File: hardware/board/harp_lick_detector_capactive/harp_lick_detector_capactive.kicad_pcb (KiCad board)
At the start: 2 copper layers, 90 x 60 mm, 119 parts, among them J1 USB_C_Receptacle_USB2.0, J10 Conn_01x02_Male, J2 Conn_01x03_Male, J3 Conn_01x03_Male, J4 AudioJack3, J5 Barrel_Jack_Switch, J6 Conn_Coaxial, J7 Conn_Coaxial, J8 Conn_Coaxial, J9 Conn_Coaxial, U10 LTC6263, U11 CD74AC04, U2 W25Q128JVS, U3 ADUM4160, U4 TPD2EUSB30, U5 LT3030, U6 LM27762, U7 AD9833xRM, U8 LTC6263, U9 LTC6268xS6-10, X1 ECS-TXO-2016, X2 ASE-25.000MHZ-L-C-T

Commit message: loosely place components
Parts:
- removed REF** (x4): MountingHole_3.2mm_M3_DIN965, MountingHole:MountingHole_3.2mm_M3_DIN965
- added U1: RP2040, machine_agency_components:RP2040-QFN-56, F.Cu at (197.0, 79.8)
- C10, C11, C12, C13, C14, C17, C18, C19, C20, C21, C22, C23, C24, C27, C28, C29, C30, C32, C33, C34, C35, C36: footprint Capacitor_SMD:C_0603_1608Metric_Pad1.08x0.95mm_HandSolder -> Capacitor_SMD:C_0402_1005Metric_Pad0.74x0.62mm_HandSolder
- moved R20 205.3 mm to (226.5, 62.5), turned to 180 degrees
- moved R32 198.2 mm to (240.2, 102.0), turned to 180 degrees
- moved R31 196.5 mm to (240.2, 97.4), turned to 180 degrees
- moved D3 193.1 mm to (230.0, 75.0)
- moved R4 191.8 mm to (223.1, 88.1)
- moved C10 184.7 mm to (219.2, 86.0), turned to 90 degrees
- moved R8 183.3 mm to (205.7, 80.5), turned to 180 degrees
- moved R7 183.0 mm to (220.0, 81.5), turned to 180 degrees
- moved C16 181.8 mm to (222.0, 98.6), turned to 180 degrees
- moved C36 177.9 mm to (219.8, 50.9)
- moved R22 175.0 mm to (226.5, 75.0), turned to 180 degrees
- moved R5 174.3 mm to (221.4, 75.1), turned to 180 degrees
- moved C22 174.0 mm to (215.7, 50.8)
- moved C108 173.7 mm to (202.9, 78.6)
- moved R6 173.2 mm to (220.0, 80.5), turned to 180 degrees
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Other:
- board size 90 x 60 mm -> 68 x 60 mm

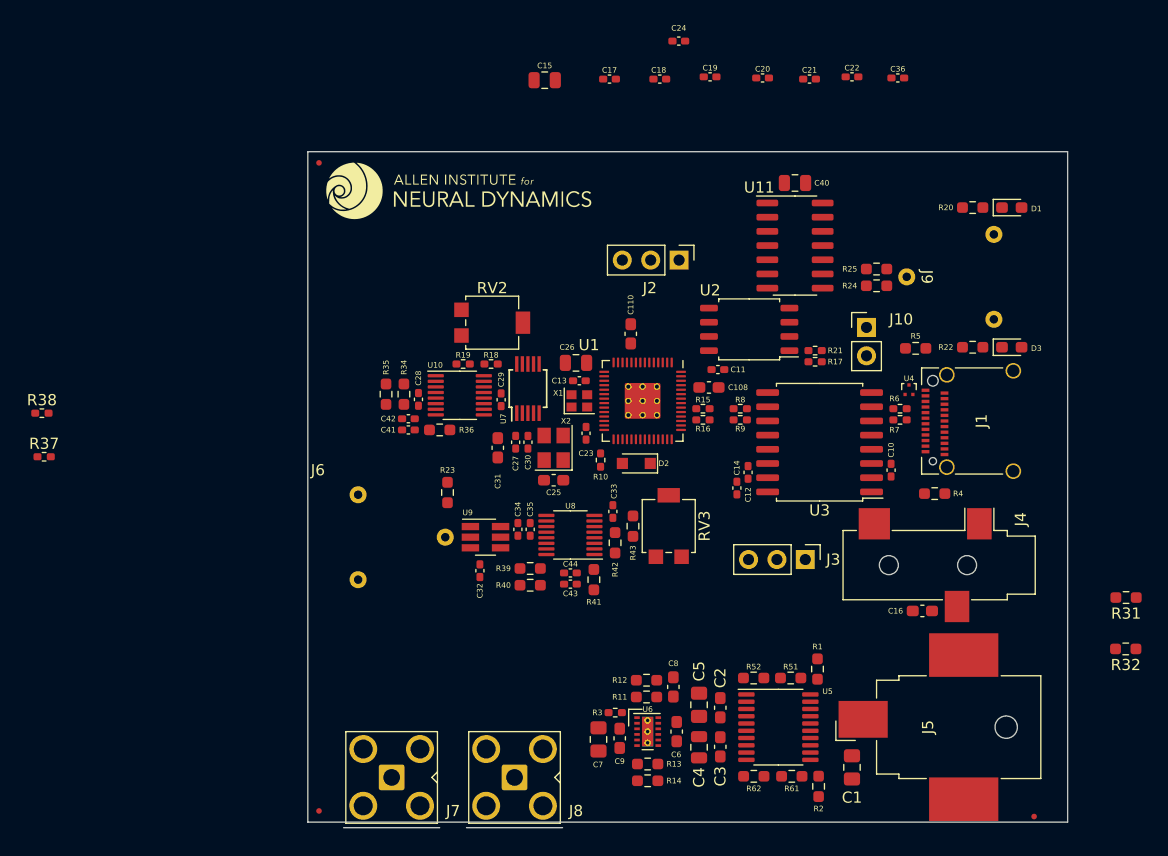
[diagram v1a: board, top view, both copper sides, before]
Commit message: change usb connector; more layout
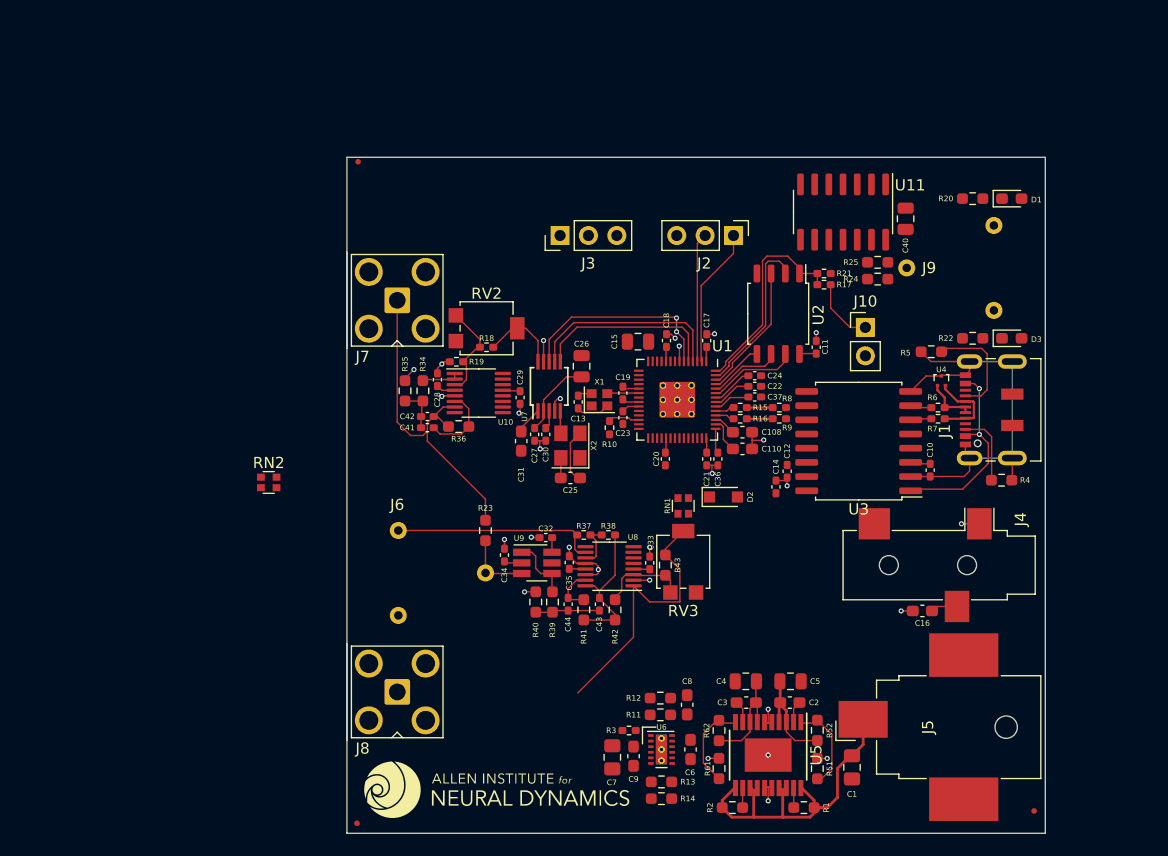
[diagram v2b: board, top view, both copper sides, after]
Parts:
- removed R31, R32: 4K7, Resistor_SMD:R_0603_1608Metric_Pad0.98x0.95mm_HandSolder
- added C37: 100nF, Capacitor_SMD:C_0402_1005Metric_Pad0.74x0.62mm_HandSolder, F.Cu at (207.0, 79.5)
- added RN1: 5K, Resistor_SMD:R_Array_Convex_2x0606, F.Cu at (200.6, 89.2)
- added RN2: 5K, Resistor_SMD:R_Array_Convex_2x0606, F.Cu at (163.5, 87.1)
- C5: footprint Capacitor_SMD:C_0805_2012Metric_Pad1.18x1.45mm_HandSolder -> Capacitor_SMD:C_0805_2012Metric
- J1: footprint Connector_USB:USB_C_Receptacle_Amphenol_12401610E4-2A_CircularHoles -> Connector_USB:USB_C_Receptacle_JAE_DX07S016JA1R1500
- U5: footprint Package_SO:TSSOP-20_4.4x6.5mm_P0.65mm -> Package_SO:ETSSOP-20-1EP_4.4x6.5mm_P0.65mm_EP3x4.2mm
- moved G*** 53.7 mm to (183.9, 114.6)
- moved R38 51.9 mm to (193.9, 91.8)
- moved R37 48.8 mm to (191.7, 91.8), turned to 180 degrees
- moved J7 42.7 mm to (175.0, 70.8), turned to 90 degrees
- moved C36 37.7 mm to (203.7, 85.0), turned to 90 degrees
- moved J3 36.4 mm to (189.6, 65.0), turned to 90 degrees
- moved C21 35.2 mm to (202.7, 85.0), turned to 90 degrees
- moved C20 35.2 mm to (199.0, 85.0), turned to 90 degrees
- moved C24 30.7 mm to (207.0, 77.5), turned to 180 degrees
- moved C19 29.4 mm to (195.2, 79.1), turned to -90 degrees
- moved C22 29.0 mm to (207.0, 78.5), turned to 180 degrees
- moved C17 25.0 mm to (202.7, 74.4), turned to -90 degrees
- moved C15 24.8 mm to (196.5, 74.5), turned to 180 degrees
- moved C18 23.4 mm to (199.1, 74.4), turned to -90 degrees
- moved C110 14.4 mm to (205.9, 84.1), turned to 0 degrees
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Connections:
- U2 pad 2: /MCU/QSPI_SD1 -> /MCU/QSPI_D1
- U2 pad 5: /MCU/QSPI_SD0 -> /MCU/QSPI_D0
- U8 pad 1: Net-(C43-Pad2) -> Net-(J8-Pad1)
- U8 pad 14: unconnected-(U8-Pad14) -> GND
- U8 pad 15: unconnected-(U8-Pad15) -> Net-(C44-Pad2)
- U8 pad 16: unconnected-(U8-Pad16) -> Net-(C43-Pad2)
- U8 pad 2: Net-(C44-Pad2) -> GND
- U8 pad 3: GND -> Net-(R42-Pad2)
- U8 pad 5: Net-(R42-Pad2) -> unconnected-(U8-Pad5)
- U8 pad 6: GND -> unconnected-(U8-Pad6)
- U8 pad 7: Net-(J8-Pad1) -> unconnected-(U8-Pad7)
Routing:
- net GND: track 0.00 -> 47.1 mm, vias 0 -> 27
- net +3V3: track 0.00 -> 43.4 mm
- net GND1: track 0.00 -> 37.9 mm
- net +12V: track 0.00 -> 32.4 mm
- net /100[Khz], 50[uVpp] Sine Wave/VSIN: track 0.00 -> 29.9 mm
- net Net-(J8-Pad1): track 0.00 -> 24.3 mm
- net /MCU/QSPI_CS: track 0.00 -> 18.8 mm
- net Net-(J6-Pad2): track 0.00 -> 18.6 mm
- net /CS: track 0.00 -> 18.4 mm, vias 0 -> 2
- net /SCK: track 0.00 -> 17.9 mm
- net VBUS: track 0.00 -> 17.7 mm, vias 0 -> 2
- net /PICO: track 0.00 -> 16.4 mm
- net /MCU/QSPI_D1: track 0.00 -> 14.7 mm
- net Net-(C43-Pad2): track 0.00 -> 13.0 mm
- net /MCU/UART0_TXD: track 0.00 -> 12.5 mm
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- added copper zone on In1.Cu, net GND
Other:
- board size 68 x 60 mm -> 62.5 x 60.5 mm
- copper layers 2 -> 4

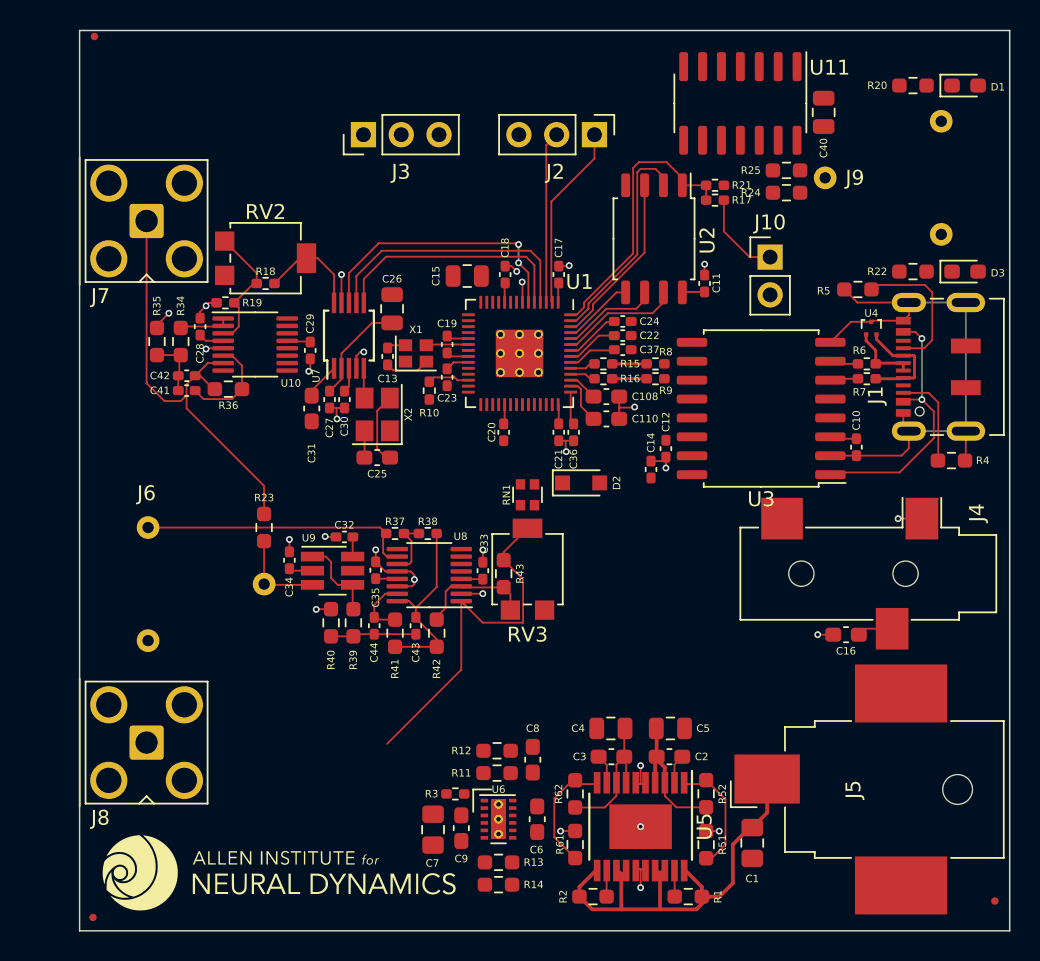
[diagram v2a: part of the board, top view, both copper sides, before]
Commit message: add analog front end test board
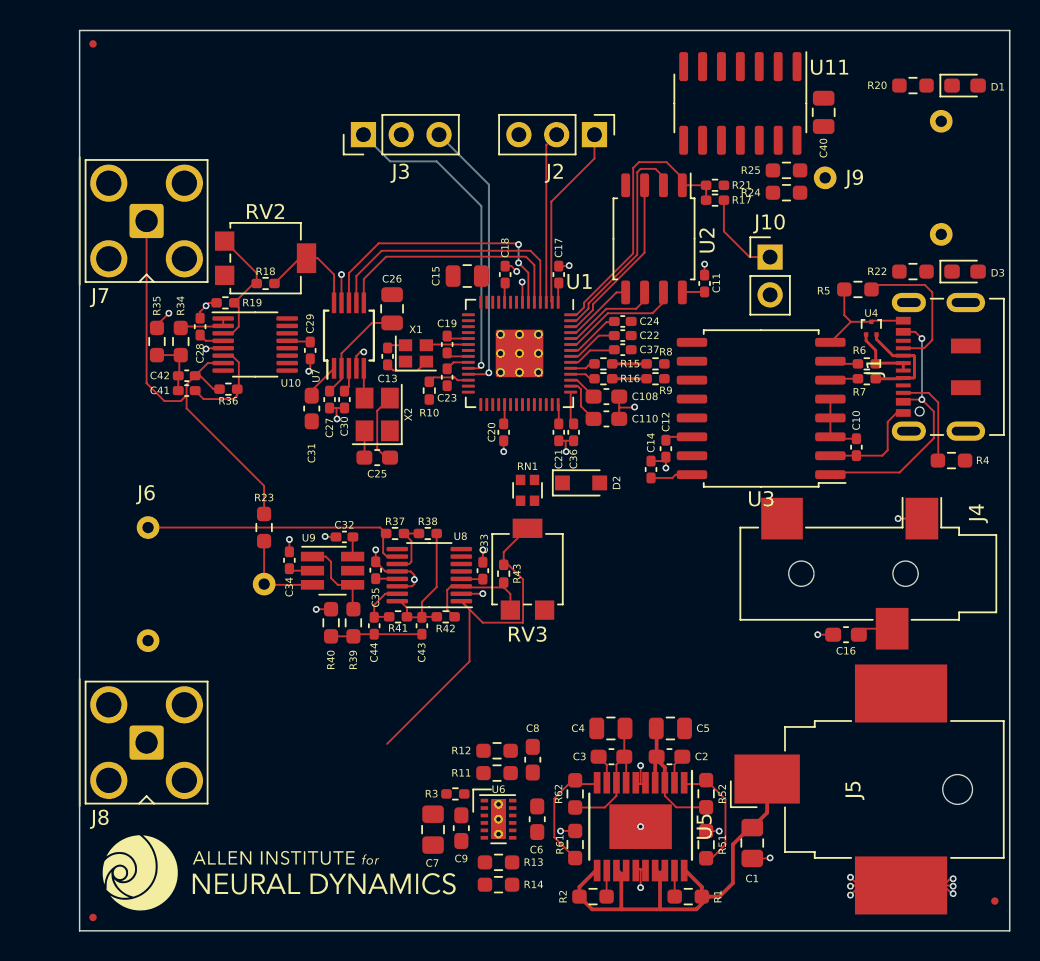
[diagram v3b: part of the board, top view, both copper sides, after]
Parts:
- R36, R41: value 200K -> 198K; footprint Resistor_SMD:R_0603_1608Metric_Pad0.98x0.95mm_HandSolder -> Resistor_SMD:R_0402_1005Metric_Pad0.72x0.64mm_HandSolder
- R42, R43: footprint Resistor_SMD:R_0603_1608Metric_Pad0.98x0.95mm_HandSolder -> Resistor_SMD:R_0402_1005Metric_Pad0.72x0.64mm_HandSolder
- moved R42 1.25 mm to (195.1, 97.4), turned to 0 degrees
- moved R41 1.12 mm to (191.9, 97.4), turned to 0 degrees
- moved FID3 0.51 mm to (171.4, 58.9)
- moved C43 0.40 mm to (193.5, 98.0)
- moved RN1 0.30 mm to (200.6, 88.9)
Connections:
- J1 pad S1: GND1 -> unconnected-(J1-PadS1)
- RN1 pad 1: Net-(J8-Pad1) -> /MCU/ADC
- RN1 pad 2: /MCU/ADC -> Net-(J8-Pad1)
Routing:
- net GND1: track 37.9 -> 15.1 mm
- net /MCU/SWCLK: track 0.00 -> 21.6 mm, vias 0 -> 1
- net GND: track 47.1 -> 67.8 mm, vias 27 -> 35
- net /MCU/SWDIO: track 0.00 -> 18.8 mm, vias 0 -> 1
- net +3V3: track 43.4 -> 47.8 mm
- net Net-(C43-Pad2): track 13.0 -> 9.51 mm
- net /MCU/VDD1: track 1.80 -> 4.34 mm
- net unconnected-(J1-PadS1): track 0.00 -> 0.53 mm
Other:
- board text added: "TODO: consider a (uh-oh) GND1 cutout of the ground plane or (better!) power plane."

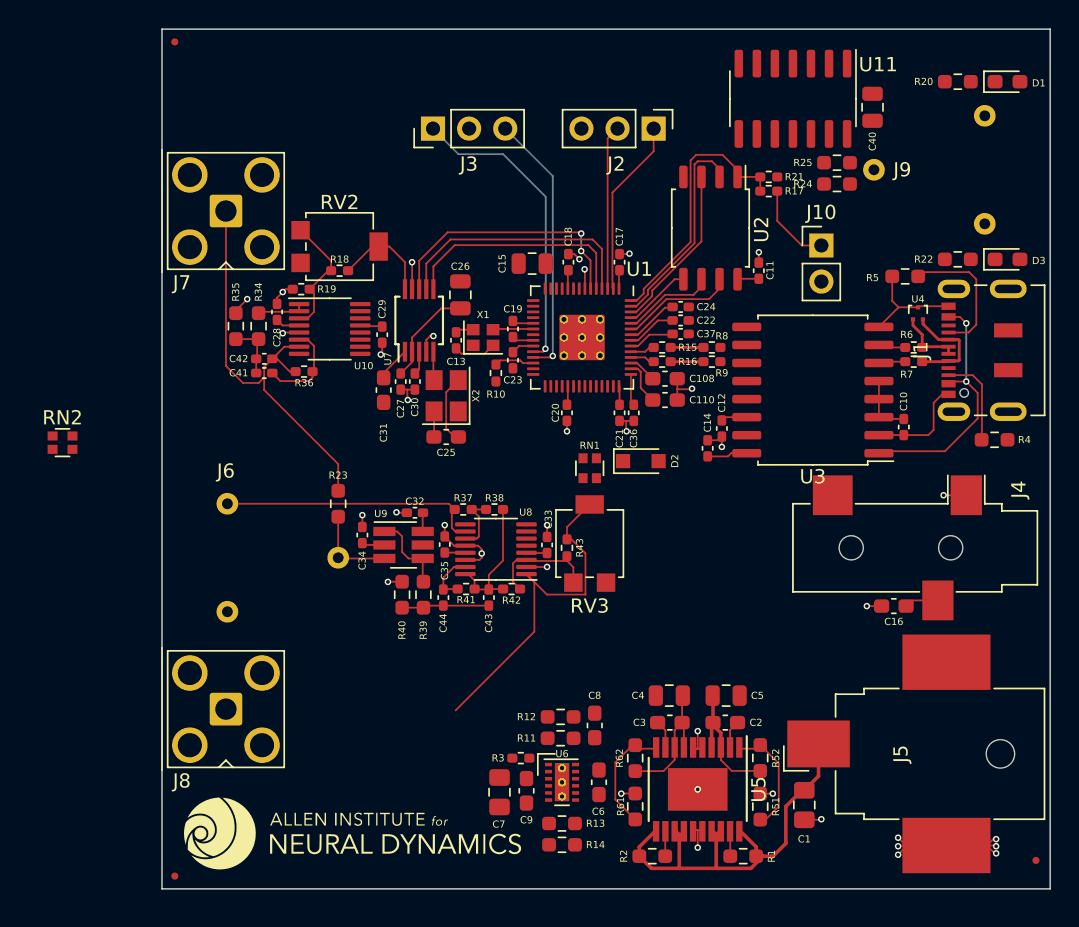
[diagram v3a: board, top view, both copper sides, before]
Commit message: make mclk frequency a parameter
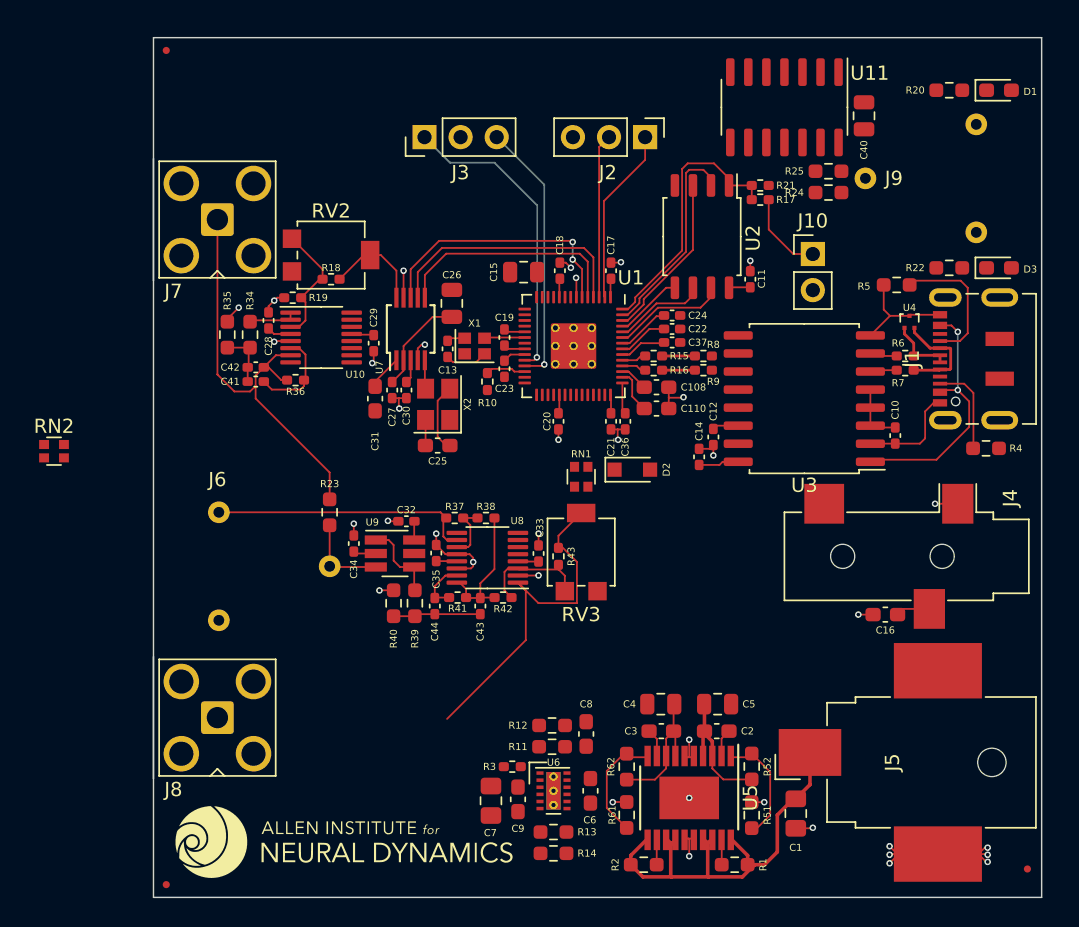
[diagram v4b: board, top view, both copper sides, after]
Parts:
- moved C27 0.85 mm to (186.7, 83.4)
- moved C3 0.85 mm to (205.6, 107.4)
- moved C30 0.85 mm to (187.7, 83.4)
- moved R19 0.85 mm to (179.7, 76.9)
- moved R62 0.85 mm to (203.2, 109.9)
- moved U10 0.85 mm to (181.7, 79.7)
- moved C15 0.85 mm to (195.9, 75.1)
- moved C32 0.85 mm to (187.7, 92.6)
- moved C44 0.85 mm to (189.7, 98.6)
- moved R11 0.85 mm to (197.9, 108.5)
- moved R12 0.85 mm to (197.9, 107.0)
- moved R34 0.85 mm to (176.7, 79.5)
- moved R5 0.85 mm to (222.2, 76.0)
- moved R61 0.85 mm to (203.2, 113.3)
- moved U3 0.85 mm to (215.7, 84.0)
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
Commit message: ship rev1 of test pcbs
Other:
- board text added: "TODO: move TVS diode in-between D+/D- pair"
- board text removed: "TODO: consider a (uh-oh) GND1 cutout of the ground plane or (better!) power plane."
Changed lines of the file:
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@@
   )
   (gr_rect (start 169.9 119.1) (end 232.4 58.6) (layer "Edge.Cuts") (width 0.1) (fill none))
-  (gr_text "TODO: consider a (uh-oh) GND1 cutout of \nthe ground plane or (better!) power plane." (at 260.6 82.6) (layer "Cmts.User")
+  (gr_text "TODO: move TVS diode in-between D+/D- pair" (at 260.6 82.6) (layer "Cmts.User")
     (effects (font (size 1.5 1.5) (thickness 0.3)))
   )
